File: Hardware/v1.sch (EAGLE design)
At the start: 79 parts, among them IC1 LM324D, IC2 m328p, IC3 REG1117, J1 22-27-2061-06, J2 22-27-2021-02, J3 22-27-2021-02, J4 22-27-2031-03, J5 22-27-2041-04, Q1 BSS123, Q2 BSS123, Q3 BSS123, Q5 BSS123

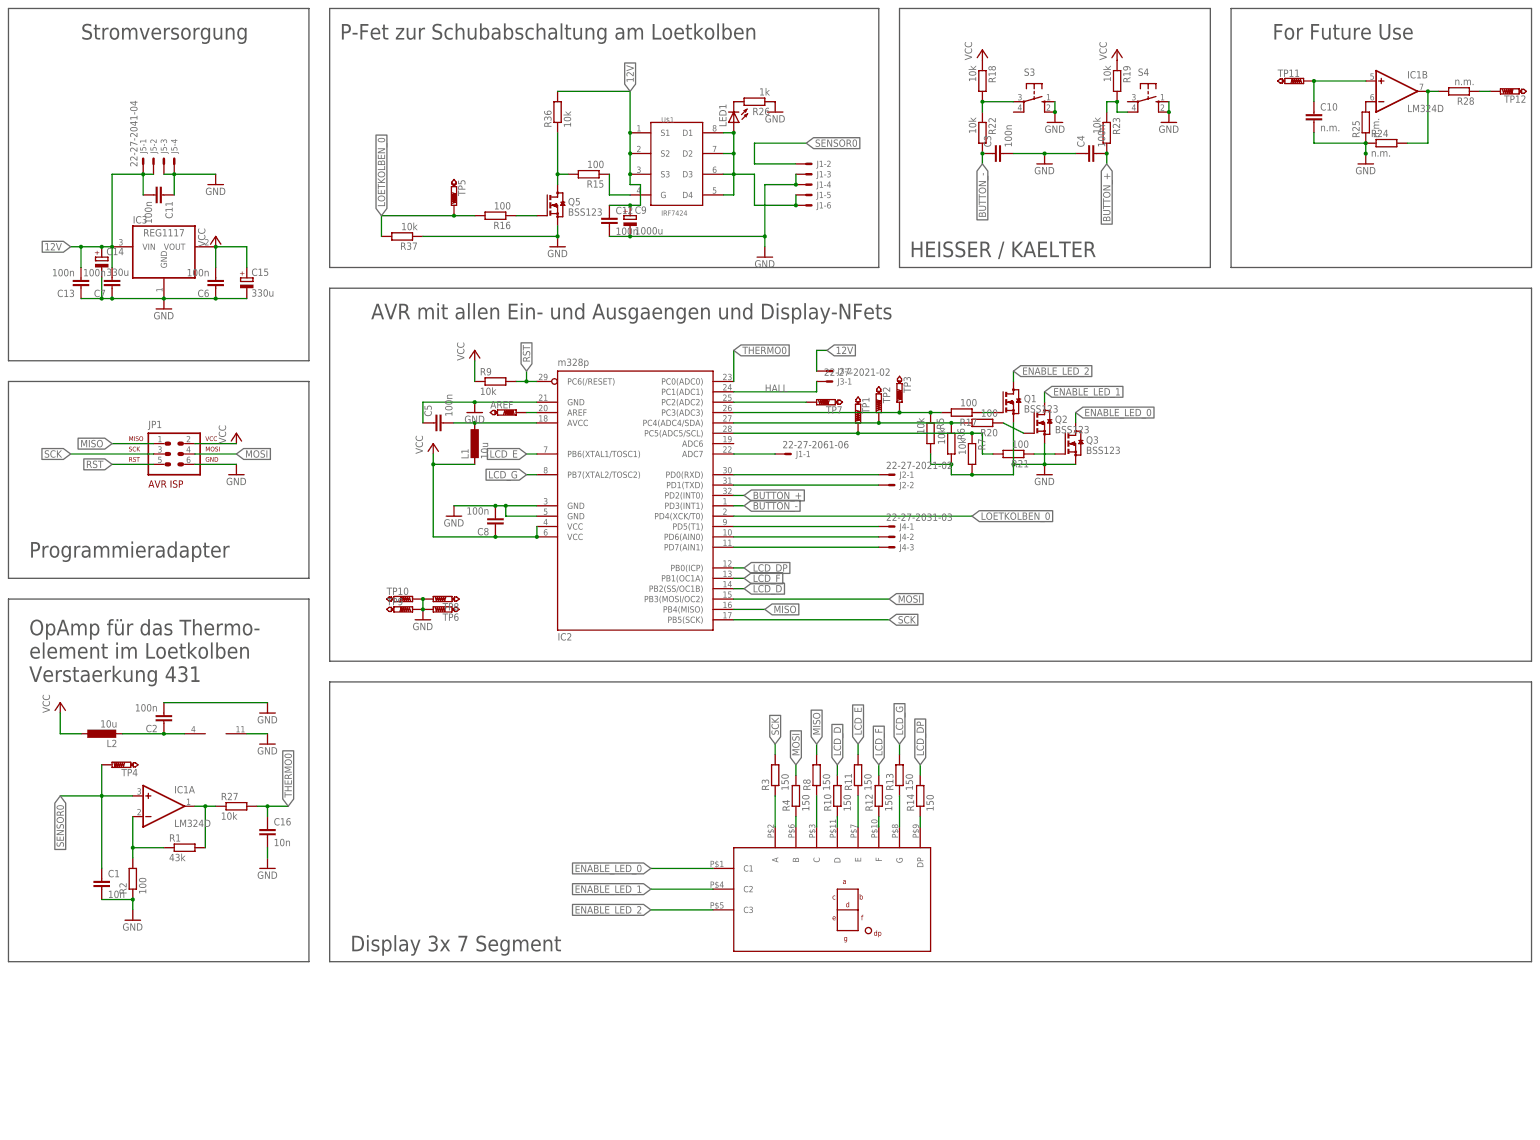
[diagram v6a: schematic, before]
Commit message: Added a 100nF cap to AREF (see issue #4). Added an extra LED to see if 5V is supplied.
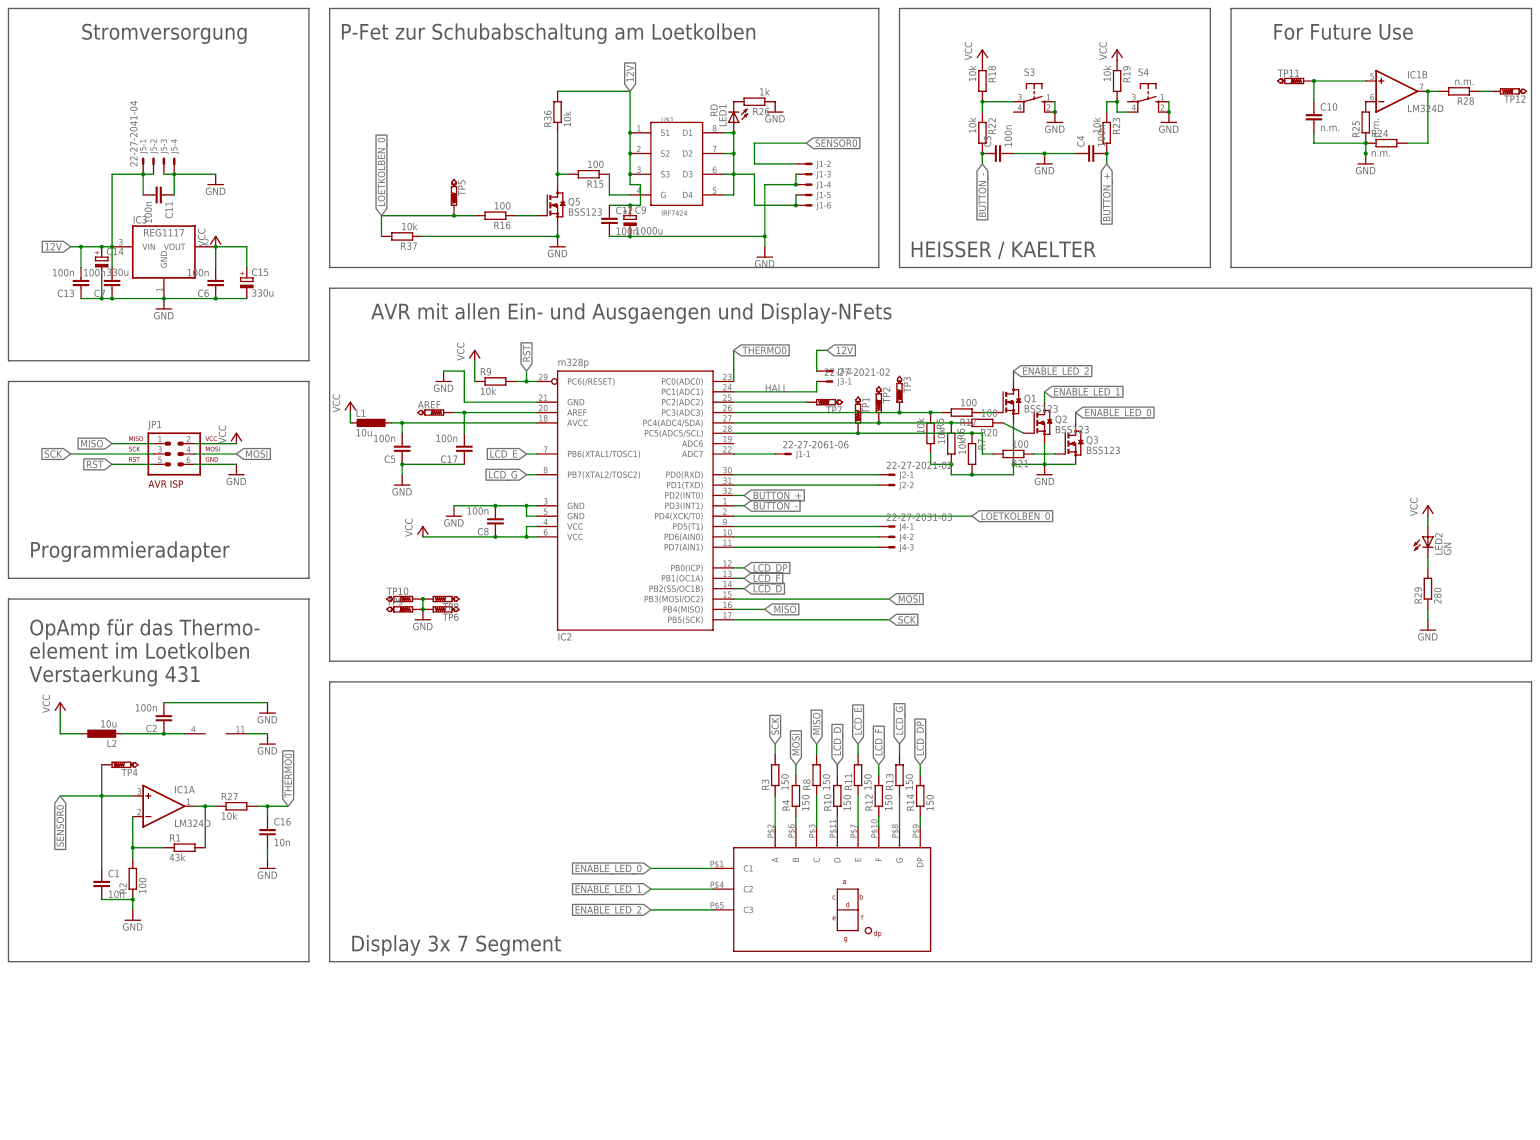
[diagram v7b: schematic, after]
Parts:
- added C17: 100n, rcl:C-EUC0603
- added LED2: GN, led:LEDCHIP-LED0805
- added R29: 280, rcl:R-EU_R0603
- LED1: value (none) -> RD
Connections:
- new net N$24: LED2.C, R29.2
- net AREF: now also C17.2
- net GND: now also C17.1, R29.1
- net VCC: now also LED2.A
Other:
- moved on the sheet: AREF, C5, L1
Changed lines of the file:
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@@
 <?xml version="1.0" encoding="utf-8"?>
 <!DOCTYPE eagle SYSTEM "eagle.dtd">
-<eagle version="6.5.0">
+<eagle version="7.2.0">
 <drawing>
 <settings>
@@
 <part name="GND14" library="supply1" deviceset="GND" device=""/>
 <part name="AREF" library="testpad" deviceset="PTR1" device="B1,27"/>
-<part name="LED1" library="led" deviceset="LED" device="CHIP-LED0805"/>
+<part name="LED1" library="led" deviceset="LED" device="CHIP-LED0805" value="RD"/>
 <part name="R26" library="rcl" deviceset="R-EU_" device="R0603" value="1k"/>
 <part name="GND18" library="supply1" deviceset="GND" device=""/>
@@
 <part name="TP7" library="testpad" deviceset="PTR1" device="B1,27"/>
 <part name="R28" library="rcl" deviceset="R-EU_" device="R0603" value="n.m."/>
+<part name="C17" library="rcl" deviceset="C-EU" device="C0603" value="100n"/>
+<part name="GND19" library="supply1" deviceset="GND" device=""/>
+<part name="P+8" library="supply1" deviceset="VCC" device=""/>
+<part name="LED2" library="led" deviceset="LED" device="CHIP-LED0805" value="GN"/>
+<part name="R29" library="rcl" deviceset="R-EU_" device="R0603" value="280"/>
+<part name="GND20" library="supply1" deviceset="GND" device=""/>
+<part name="P+9" library="supply1" deviceset="VCC" device=""/>
 </parts>
 <sheets>
@@
 <instance part="C1" gate="G$1" x="48.26" y="48.26"/>
 <instance part="IC2" gate="G$1" x="177.8" y="144.78"/>
-<instance part="GND6" gate="1" x="139.7" y="162.56"/>
+<instance part="GND6" gate="1" x="132.08" y="170.18"/>
 <instance part="GND7" gate="1" x="134.62" y="137.16"/>
 <instance part="R9" gate="G$1" x="144.78" y="170.18"/>
 <instance part="P+2" gate="VCC" x="139.7" y="177.8"/>
-<instance part="C5" gate="G$1" x="129.54" y="160.02" rot="R90"/>
-<instance part="P+3" gate="VCC" x="129.54" y="154.94"/>
+<instance part="C5" gate="G$1" x="121.92" y="152.4" rot="R180"/>
+<instance part="P+3" gate="VCC" x="109.22" y="165.1"/>
 <instance part="JP1" gate="G$1" x="66.04" y="152.4"/>
 <instance part="P+4" gate="VCC" x="81.28" y="157.48"/>
@@
 <instance part="TP5" gate="G$1" x="134.62" y="213.36" rot="R180"/>
 <instance part="GND3" gate="1" x="127" y="111.76"/>
-<instance part="L1" gate="G$1" x="139.7" y="154.94"/>
+<instance part="L1" gate="G$1" x="114.3" y="160.02" rot="R270"/>
 <instance part="L2" gate="G$1" x="48.26" y="83.82" rot="R90"/>
 <instance part="C2" gate="G$1" x="63.5" y="86.36" rot="R180"/>
@@
 <instance part="C4" gate="G$1" x="289.56" y="226.06" rot="R90"/>
 <instance part="GND14" gate="1" x="279.4" y="223.52"/>
-<instance part="AREF" gate="G$1" x="149.86" y="162.56" rot="R270"/>
+<instance part="AREF" gate="G$1" x="132.08" y="162.56" rot="R270"/>
 <instance part="LED1" gate="G$1" x="203.2" y="233.68" rot="R180"/>
 <instance part="R26" gate="G$1" x="208.28" y="238.76" rot="R180"/>
@@
 <instance part="TP7" gate="G$1" x="223.52" y="165.1" rot="R90"/>
 <instance part="R28" gate="G$1" x="381" y="241.3" rot="R180"/>
+<instance part="C17" gate="G$1" x="137.16" y="152.4" rot="R180"/>
+<instance part="GND19" gate="1" x="121.92" y="144.78"/>
+<instance part="P+8" gate="VCC" x="127" y="134.62"/>
+<instance part="LED2" gate="G$1" x="373.38" y="132.08"/>
+<instance part="R29" gate="G$1" x="373.38" y="119.38" rot="R90"/>
+<instance part="GND20" gate="1" x="373.38" y="109.22"/>
+<instance part="P+9" gate="VCC" x="373.38" y="139.7"/>
 </instances>
 <busses>
@@
 </segment>
 <segment>
+<pinref part="L1" gate="G$1" pin="2"/>
+<pinref part="P+3" gate="VCC" pin="VCC"/>
+<wire x1="109.22" y1="162.56" x2="109.22" y2="160.02" width="0.1524" layer="91"/>
+</segment>
+<segment>
 <pinref part="IC2" gate="G$1" pin="VCC@1"/>
 <pinref part="IC2" gate="G$1" pin="VCC@2"/>
-<wire x1="154.94" y1="134.62" x2="154.94" y2="132.08" width="0.1524" layer="91"/>
-<wire x1="154.94" y1="132.08" x2="144.78" y2="132.08" width="0.1524" layer="91"/>
-<wire x1="144.78" y1="132.08" x2="129.54" y2="132.08" width="0.1524" layer="91"/>
-<wire x1="129.54" y1="132.08" x2="129.54" y2="149.86" width="0.1524" layer="91"/>
-<junction x="154.94" y="132.08"/>
-<wire x1="129.54" y1="149.86" x2="139.7" y2="149.86" width="0.1524" layer="91"/>
-<pinref part="P+3" gate="VCC" pin="VCC"/>
-<wire x1="129.54" y1="152.4" x2="129.54" y2="149.86" width="0.1524" layer="91"/>
-<junction x="129.54" y="149.86"/>
+<wire x1="154.94" y1="132.08" x2="152.4" y2="132.08" width="0.1524" layer="91"/>
+<wire x1="152.4" y1="132.08" x2="144.78" y2="132.08" width="0.1524" layer="91"/>
+<wire x1="144.78" y1="132.08" x2="127" y2="132.08" width="0.1524" layer="91"/>
 <pinref part="C8" gate="G$1" pin="1"/>
 <junction x="144.78" y="132.08"/>
-<pinref part="L1" gate="G$1" pin="2"/>
+<pinref part="P+8" gate="VCC" pin="VCC"/>
+<wire x1="152.4" y1="132.08" x2="152.4" y2="134.62" width="0.1524" layer="91"/>
+<junction x="152.4" y="132.08"/>
+<wire x1="152.4" y1="134.62" x2="154.94" y2="134.62" width="0.1524" layer="91"/>
 </segment>
 <segment>
@@
 <pinref part="P+7" gate="VCC" pin="VCC"/>
 </segment>
+<segment>
+<pinref part="P+9" gate="VCC" pin="VCC"/>
+<pinref part="LED2" gate="G$1" pin="A"/>
+<wire x1="373.38" y1="134.62" x2="373.38" y2="137.16" width="0.1524" layer="91"/>
+</segment>
 </net>
 <net name="GND" class="0">
@@
 <pinref part="IC2" gate="G$1" pin="GND@1"/>
 <pinref part="GND7" gate="1" pin="GND"/>
-<wire x1="154.94" y1="139.7" x2="147.32" y2="139.7" width="0.1524" layer="91"/>
+<wire x1="154.94" y1="139.7" x2="152.4" y2="139.7" width="0.1524" layer="91"/>
 <pinref part="IC2" gate="G$1" pin="GND@2"/>
-<wire x1="147.32" y1="139.7" x2="144.78" y2="139.7" width="0.1524" layer="91"/>
+<wire x1="152.4" y1="139.7" x2="144.78" y2="139.7" width="0.1524" layer="91"/>
 <wire x1="144.78" y1="139.7" x2="134.62" y2="139.7" width="0.1524" layer="91"/>
-<wire x1="154.94" y1="137.16" x2="147.32" y2="137.16" width="0.1524" layer="91"/>
-<wire x1="147.32" y1="137.16" x2="147.32" y2="139.7" width="0.1524" layer="91"/>
-<junction x="147.32" y="139.7"/>
+<wire x1="154.94" y1="137.16" x2="152.4" y2="137.16" width="0.1524" layer="91"/>
+<wire x1="152.4" y1="137.16" x2="152.4" y2="139.7" width="0.1524" layer="91"/>
+<junction x="152.4" y="139.7"/>
 <pinref part="C8" gate="G$1" pin="2"/>
 <junction x="144.78" y="139.7"/>
 </segment>
 <segment>
+<pinref part="C5" gate="G$1" pin="1"/>
+<pinref part="GND19" gate="1" pin="GND"/>
+<wire x1="121.92" y1="147.32" x2="121.92" y2="149.86" width="0.1524" layer="91"/>
+<pinref part="C17" gate="G$1" pin="1"/>
+<wire x1="121.92" y1="149.86" x2="137.16" y2="149.86" width="0.1524" layer="91"/>
+<junction x="121.92" y="149.86"/>
+</segment>
+<segment>
 <pinref part="GND6" gate="1" pin="GND"/>
 <pinref part="IC2" gate="G$1" pin="GND"/>
-<wire x1="139.7" y1="165.1" x2="154.94" y2="165.1" width="0.1524" layer="91"/>
-<pinref part="C5" gate="G$1" pin="1"/>
-<wire x1="127" y1="160.02" x2="127" y2="165.1" width="0.1524" layer="91"/>
-<wire x1="127" y1="165.1" x2="139.7" y2="165.1" width="0.1524" layer="91"/>
-<junction x="139.7" y="165.1"/>
+<wire x1="132.08" y1="172.72" x2="137.16" y2="172.72" width="0.1524" layer="91"/>
+<wire x1="137.16" y1="172.72" x2="137.16" y2="165.1" width="0.1524" layer="91"/>
+<wire x1="137.16" y1="165.1" x2="154.94" y2="165.1" width="0.1524" layer="91"/>
 </segment>
 <segment>
@@
 <pinref part="GND17" gate="1" pin="GND"/>
 <wire x1="88.9" y1="55.88" x2="88.9" y2="53.34" width="0.1524" layer="91"/>
+</segment>
+<segment>
+<pinref part="R29" gate="G$1" pin="1"/>
+<pinref part="GND20" gate="1" pin="GND"/>
+<wire x1="373.38" y1="111.76" x2="373.38" y2="114.3" width="0.1524" layer="91"/>
 </segment>
 </net>
@@
 <segment>
 <pinref part="IC2" gate="G$1" pin="AVCC"/>
-<wire x1="139.7" y1="160.02" x2="154.94" y2="160.02" width="0.1524" layer="91"/>
-<junction x="139.7" y="160.02"/>
+<wire x1="119.38" y1="160.02" x2="121.92" y2="160.02" width="0.1524" layer="91"/>
 <pinref part="L1" gate="G$1" pin="1"/>
 <pinref part="C5" gate="G$1" pin="2"/>
-<wire x1="134.62" y1="160.02" x2="139.7" y2="160.02" width="0.1524" layer="91"/>
+<wire x1="121.92" y1="160.02" x2="154.94" y2="160.02" width="0.1524" layer="91"/>
+<wire x1="121.92" y1="157.48" x2="121.92" y2="160.02" width="0.1524" layer="91"/>
+<junction x="121.92" y="160.02"/>
 </segment>
 </net>
@@
 <pinref part="IC2" gate="G$1" pin="AREF"/>
 <pinref part="AREF" gate="G$1" pin="TP"/>
-<wire x1="152.4" y1="162.56" x2="154.94" y2="162.56" width="0.1524" layer="91"/>
+<wire x1="134.62" y1="162.56" x2="137.16" y2="162.56" width="0.1524" layer="91"/>
+<pinref part="C17" gate="G$1" pin="2"/>
+<wire x1="137.16" y1="162.56" x2="154.94" y2="162.56" width="0.1524" layer="91"/>
+<wire x1="137.16" y1="157.48" x2="137.16" y2="162.56" width="0.1524" layer="91"/>
+<junction x="137.16" y="162.56"/>
 </segment>
 </net>
@@
 </segment>
 </net>
+<net name="N$24" class="0">
+<segment>
+<pinref part="LED2" gate="G$1" pin="C"/>
+<pinref part="R29" gate="G$1" pin="2"/>
+<wire x1="373.38" y1="124.46" x2="373.38" y2="127" width="0.1524" layer="91"/>
+</segment>
+</net>

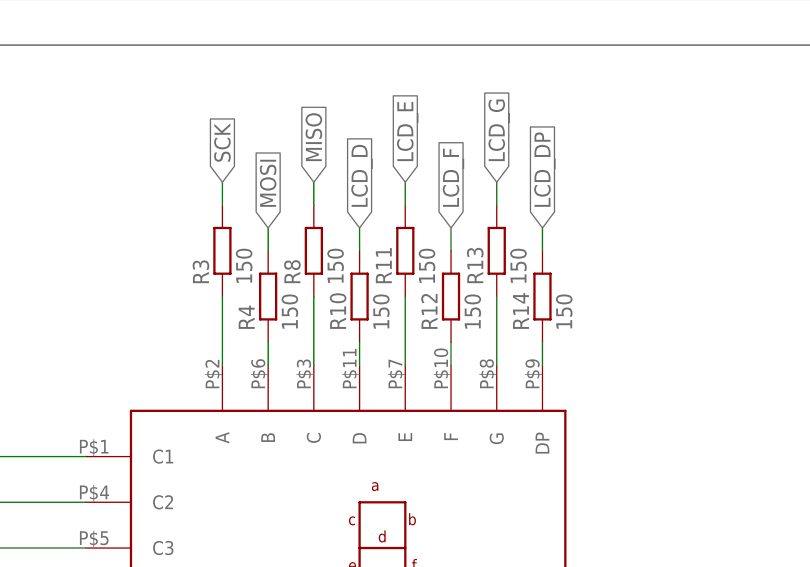
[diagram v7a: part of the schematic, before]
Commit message: Changed resistors at the LED display to 300 Ohm to reduce power drain under 5V supply. Changed the position of the LED showing the duty cycle of the p-fet slightly to make it easier to solder it on.
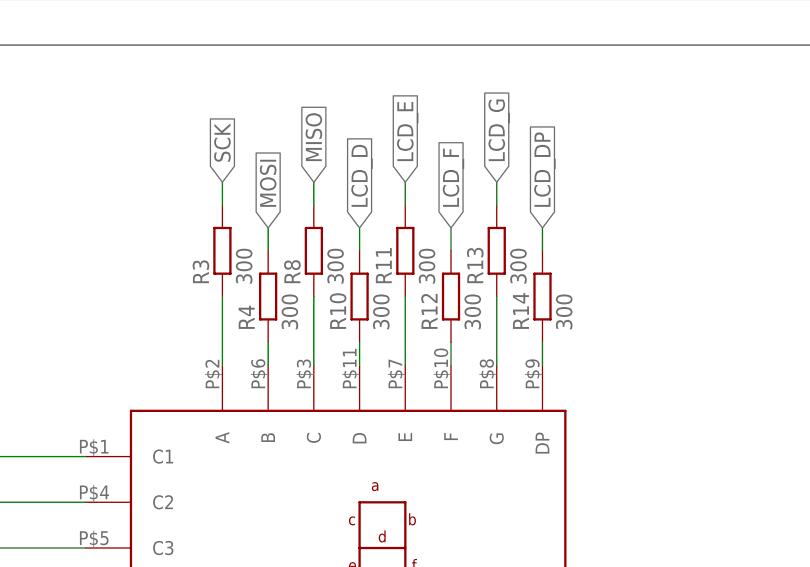
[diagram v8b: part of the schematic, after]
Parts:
- R10, R11, R12, R13, R14, R3, R4, R8: value 150 -> 300
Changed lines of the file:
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@@
 <part name="C2" library="rcl" deviceset="C-EU" device="C0603" value="100n"/>
 <part name="GND12" library="supply1" deviceset="GND" device=""/>
-<part name="R3" library="rcl" deviceset="R-EU_" device="R0603" value="150"/>
-<part name="R4" library="rcl" deviceset="R-EU_" device="R0603" value="150"/>
-<part name="R8" library="rcl" deviceset="R-EU_" device="R0603" value="150"/>
-<part name="R10" library="rcl" deviceset="R-EU_" device="R0603" value="150"/>
-<part name="R11" library="rcl" deviceset="R-EU_" device="R0603" value="150"/>
-<part name="R12" library="rcl" deviceset="R-EU_" device="R0603" value="150"/>
-<part name="R13" library="rcl" deviceset="R-EU_" device="R0603" value="150"/>
-<part name="R14" library="rcl" deviceset="R-EU_" device="R0603" value="150"/>
+<part name="R3" library="rcl" deviceset="R-EU_" device="R0603" value="300"/>
+<part name="R4" library="rcl" deviceset="R-EU_" device="R0603" value="300"/>
+<part name="R8" library="rcl" deviceset="R-EU_" device="R0603" value="300"/>
+<part name="R10" library="rcl" deviceset="R-EU_" device="R0603" value="300"/>
+<part name="R11" library="rcl" deviceset="R-EU_" device="R0603" value="300"/>
+<part name="R12" library="rcl" deviceset="R-EU_" device="R0603" value="300"/>
+<part name="R13" library="rcl" deviceset="R-EU_" device="R0603" value="300"/>
+<part name="R14" library="rcl" deviceset="R-EU_" device="R0603" value="300"/>
 <part name="R15" library="rcl" deviceset="R-EU_" device="R0603" value="100"/>
 <part name="R17" library="rcl" deviceset="R-EU_" device="R0603" value="100"/>
